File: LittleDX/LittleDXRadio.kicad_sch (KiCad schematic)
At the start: 91 parts, among them J12 Conn_Coaxial, J17 Filt1, J18 Filt2, Q12 MMBT2222, Q13 SS8550, Q15 NC, Q3 2N7000, Q5 NC, Q6 2N7000, Q7 2N7000, Q8 SS8550, Q9 2N7000, T3 Current, U6 SI5351A, U8 Si4735-D60-GU, Y3 25 MHz

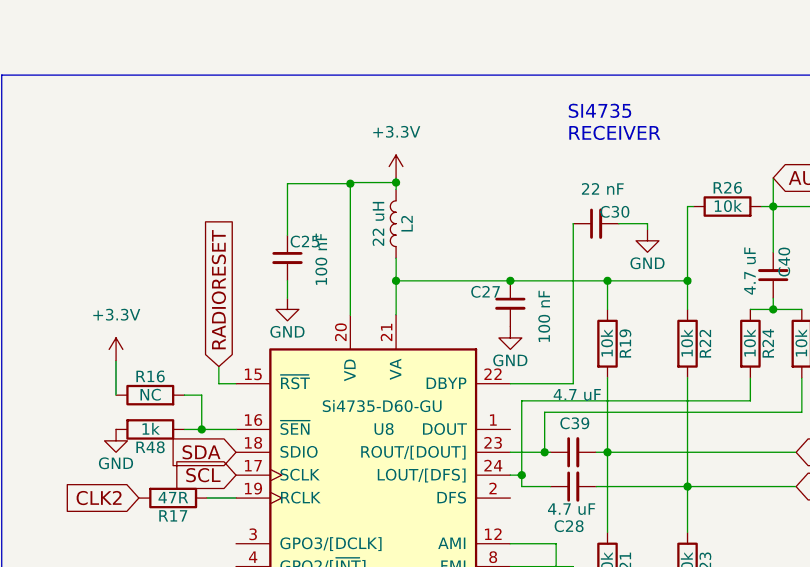
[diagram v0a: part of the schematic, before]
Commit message: Small moving around of components
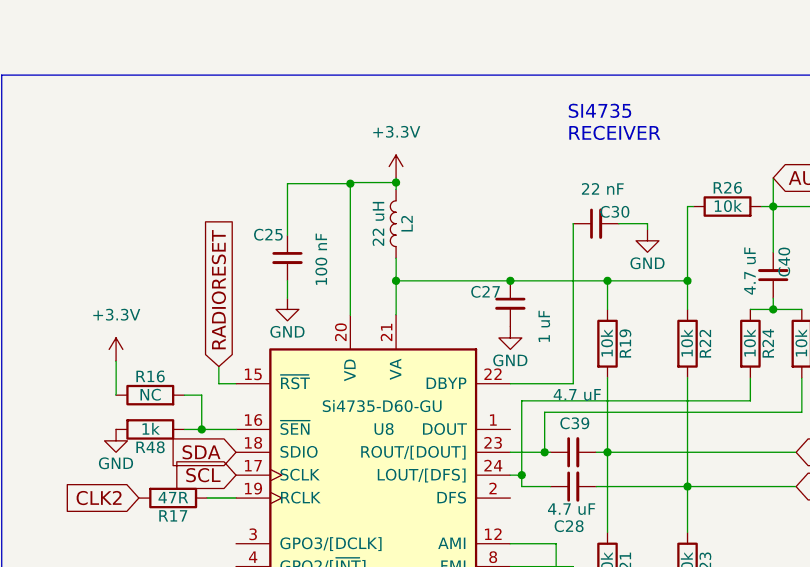
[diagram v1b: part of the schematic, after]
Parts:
- C27: value 100 nF -> 1 uF; LCSC C49678 -> C28323
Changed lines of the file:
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@@
   (symbol (lib_id "LittleDX-rescue:C_Small") (at 89.535 105.41 0) (unit 1)
     (in_bom yes) (on_board yes)
-    (property "Reference" "C25" (id 0) (at 89.789 103.632 0)
+    (property "Reference" "C25" (id 0) (at 85.725 102.87 0)
       (effects (font (size 1.27 1.27)) (justify left))
     )
@@
       (effects (font (size 1.27 1.27)) (justify left))
     )
-    (property "Value" "100 nF" (id 1) (at 118.11 114.935 90)
+    (property "Value" "1 uF" (id 1) (at 118.11 114.935 90)
       (effects (font (size 1.27 1.27)) (justify left))
     )
@@
       (effects (font (size 1.27 1.27)) hide)
     )
-    (property "LCSC" "C49678" (id 4) (at 114.3 110.49 0)
+    (property "LCSC" "C28323" (id 4) (at 114.3 110.49 0)
       (effects (font (size 1.524 1.524)) hide)
     )

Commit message: JLCPCB version 2
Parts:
- added C49: 100 nF, Capacitor_SMD:C_0805_2012Metric_Pad1.18x1.45mm_HandSolder, symbol LittleDX-rescue:C_Small
- added C50, C51: NC, Capacitor_SMD:C_0805_2012Metric_Pad1.18x1.45mm_HandSolder, symbol LittleDX-rescue:C_Small
- added D13, D14: 1N4148, Diode_SMD:D_SOD-123, symbol LittleDX-rescue:D
- added R36, R37: 1k, Resistor_SMD:R_0805_2012Metric_Pad1.20x1.40mm_HandSolder, symbol LittleDX-rescue:R
- added R54, R55: 10k, Resistor_SMD:R_0805_2012Metric_Pad1.20x1.40mm_HandSolder, symbol LittleDX-rescue:R
- added U9: LM358, Package_SO:SOP-8_3.9x4.9mm_P1.27mm, symbol LittleDX-rescue:LM358
- added Y4: 32.768 kHz (NC), Crystal:Crystal_SMD_3215-2Pin_3.2x1.5mm, symbol Device:Crystal
- C27: value 1 uF -> 4.7 uF; LCSC C28323 -> C1779
- C40: value 4.7 uF -> 100 nF; LCSC C1779 -> C49678
- R22, R25: value 10k -> 220k; LCSC C17414 -> C17556
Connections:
- net +3.3V: now also D13.1 (K), D14.1 (K)
- net +5V: now also C40.1, U9.8 (V+)
- net AUDIO: now also R19.1, R24.2; no longer C40.2, R26.2, R27.1
- net GND: now also C40.2, C49.2, C50.2, C51.2, R36.2, R37.2, U9.4 (V-); no longer C30.2, R23.2, R27.2
- net LCH: now also D14.2 (A), R55.2; no longer C28.2, R22.2, R23.1
- net RCH: now also D13.2 (A), R54.2; no longer C39.2, R19.2, R21.1
- net at C27.1, L2.1, U8.21 (VA): now also C30.1, R23.1; no longer R19.1, R22.1, R26.1
- net at U8.22 (DBYP): now also C30.2; no longer C30.1
- net at R17.1, U8.19 (RCLK): now also C50.1, Y4.1
- net at C28.1, U8.24 (LOUT/[DFS]): no longer R24.2
- net at C39.1, U8.23 (ROUT/[DOUT]): no longer R25.2
- net at R24.1, R25.1: now also R36.1, R54.1, U9.7; no longer C40.1
- net at U8.3 (GPO3/[DCLK]): now also C51.1, Y4.2
- new net: R19.2, R22.1, R37.1, R55.1, U9.1
- new net: C28.2, R27.1
- new net: R22.2, R27.2, U9.2 (-)
- new net: C49.1, R21.1, R23.2, U9.3 (+), U9.5 (+)
- new net: R25.2, R26.1, U9.6 (-)
- new net: C39.2, R26.2
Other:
- note added: "Little DX"
- note removed: "ARDUINO OOK/FSK TRANSMISSION RECEPTION 40/80 METER BAND DRAFT V3 BY KW4TI"
- moved on the sheet: C25, C27, C28, C30, C33, C35, C39, D10, D11, D7, D9, JP3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
